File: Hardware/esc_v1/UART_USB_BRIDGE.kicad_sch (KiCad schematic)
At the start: 11 parts, among them U5 CP2102N-Axx-xQFN24

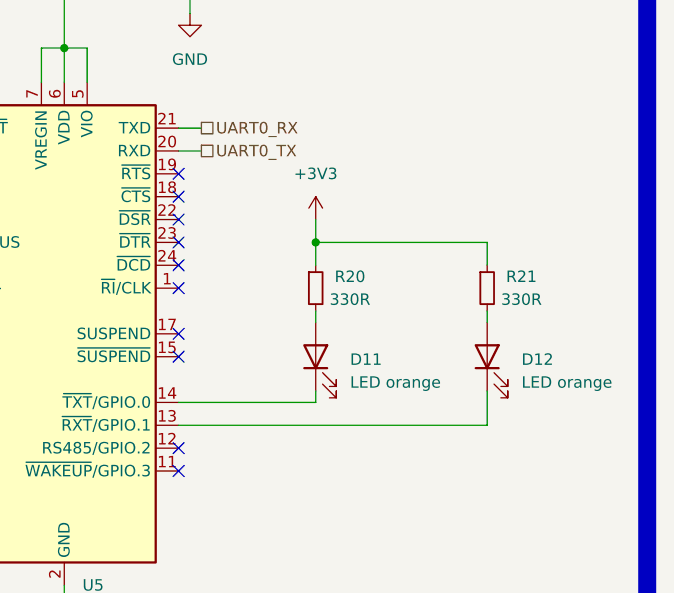
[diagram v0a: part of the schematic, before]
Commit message: changed gate driver, removed 10V buck and 5V LDO, added 5V buck. Started on Layout
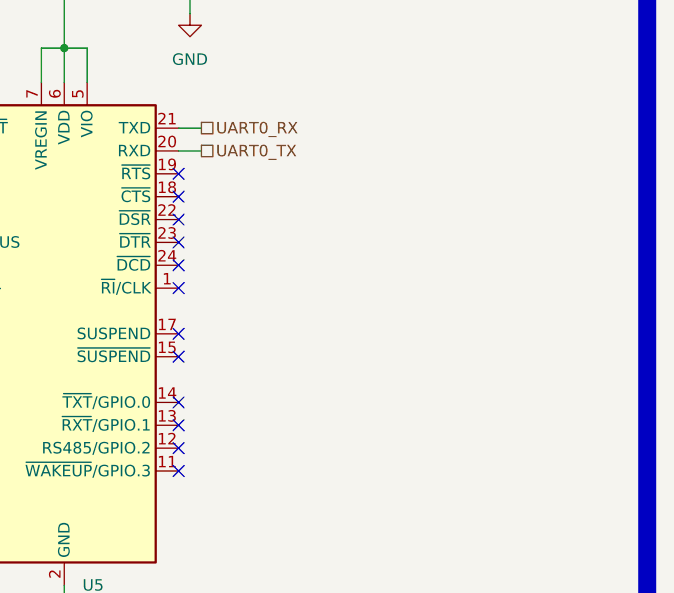
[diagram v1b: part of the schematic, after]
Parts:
- removed D11, D12: LED orange, LED_SMD:LED_0603_1608Metric, symbol Device:LED
- removed R20, R21: 330R, Resistor_SMD:R_0603_1608Metric, symbol Device:R_Small
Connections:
- no-connect marks 10 -> 12
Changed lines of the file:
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@@
   (title_block
     (title "UART to USB bridge")
-    (date "2022-07-21")
+    (date "2022-08-13")
     (rev "1")
-  )
-  (junction (at 179.07 95.25) (diameter 0) (color 0 0 0 0)
   )
   (junction (at 151.13 73.66) (diameter 0) (color 0 0 0 0)
@@
   (no_connect (at 163.83 120.65))
   (no_connect (at 163.83 118.11))
+  (no_connect (at 163.83 115.57))
+  (no_connect (at 163.83 113.03))
   (no_connect (at 163.83 107.95))
   (no_connect (at 163.83 92.71))
@@
   (no_connect (at 163.83 105.41))
   (no_connect (at 163.83 100.33))
-  (wire (pts (xy 198.12 115.57) (xy 198.12 111.76))
-    (stroke (width 0) (type default) (color 0 0 0 0))
-  )
   (wire (pts (xy 158.75 54.61) (xy 171.45 54.61))
     (stroke (width 0) (type default) (color 0 0 0 0))
@@
     (stroke (width 0) (type default) (color 0 0 0 0))
   )
-  (wire (pts (xy 163.83 115.57) (xy 198.12 115.57))
-    (stroke (width 0) (type default) (color 0 0 0 0))
-  )
   (polyline (pts (xy 38.1 38.1) (xy 38.1 73.66))
     (stroke (width 2) (type solid) (color 0 0 0 0))
   )
-  (wire (pts (xy 179.07 111.76) (xy 179.07 113.03))
-    (stroke (width 0) (type default) (color 0 0 0 0))
-  )
-  (wire (pts (xy 198.12 95.25) (xy 198.12 97.79))
-    (stroke (width 0) (type default) (color 0 0 0 0))
-  )
   (wire (pts (xy 113.03 85.09) (xy 118.11 85.09))
     (stroke (width 0) (type default) (color 0 0 0 0))
@@
     (stroke (width 2) (type solid) (color 0 0 0 0))
   )
-  (wire (pts (xy 179.07 113.03) (xy 163.83 113.03))
-    (stroke (width 0) (type default) (color 0 0 0 0))
-  )
   (wire (pts (xy 55.88 54.61) (xy 55.88 52.07))
     (stroke (width 0) (type default) (color 0 0 0 0))
   )
-  (wire (pts (xy 179.07 95.25) (xy 198.12 95.25))
-    (stroke (width 0) (type default) (color 0 0 0 0))
-  )
   (polyline (pts (xy 215.9 152.4) (xy 215.9 38.1))
     (stroke (width 2) (type solid) (color 0 0 0 0))
   )
-  (wire (pts (xy 198.12 102.87) (xy 198.12 104.14))
-    (stroke (width 0) (type default) (color 0 0 0 0))
-  )
   (wire (pts (xy 135.89 62.23) (xy 135.89 82.55))
     (stroke (width 0) (type default) (color 0 0 0 0))
@@
     (stroke (width 0) (type default) (color 0 0 0 0))
   )
-  (wire (pts (xy 179.07 95.25) (xy 179.07 97.79))
-    (stroke (width 0) (type default) (color 0 0 0 0))
-  )
   (wire (pts (xy 163.83 82.55) (xy 166.37 82.55))
     (stroke (width 0) (type default) (color 0 0 0 0))
@@
     (stroke (width 0) (type default) (color 0 0 0 0))
   )
-  (wire (pts (xy 179.07 102.87) (xy 179.07 104.14))
-    (stroke (width 0) (type default) (color 0 0 0 0))
-  )
   (wire (pts (xy 135.89 97.79) (xy 138.43 97.79))
     (stroke (width 0) (type default) (color 0 0 0 0))
   )
   (wire (pts (xy 135.89 100.33) (xy 138.43 100.33))
-    (stroke (width 0) (type default) (color 0 0 0 0))
-  )
-  (wire (pts (xy 179.07 92.71) (xy 179.07 95.25))
     (stroke (width 0) (type default) (color 0 0 0 0))
   )
@@
     )
     (property "Datasheet" "~" (id 3) (at 118.11 88.9 0)
-      (effects (font (size 1.27 1.27)) hide)
-    )
-    (pin "1")
-    (pin "2")
-  )
-  (symbol (lib_id "Device:LED") (at 179.07 107.95 90) (unit 1)
-    (in_bom yes) (on_board yes) (fields_autoplaced)
-    (property "Reference" "D11" (id 0) (at 182.88 108.2674 90)
-      (effects (font (size 1.27 1.27)) (justify right))
-    )
-    (property "Value" "LED orange" (id 1) (at 182.88 110.8074 90)
-      (effects (font (size 1.27 1.27)) (justify right))
-    )
-    (property "Footprint" "LED_SMD:LED_0603_1608Metric" (id 2) (at 179.07 107.95 0)
-      (effects (font (size 1.27 1.27)) hide)
-    )
-    (property "Datasheet" "~" (id 3) (at 179.07 107.95 0)
-      (effects (font (size 1.27 1.27)) hide)
-    )
-    (pin "1")
-    (pin "2")
-  )
-  (symbol (lib_id "Device:LED") (at 198.12 107.95 90) (unit 1)
-    (in_bom yes) (on_board yes) (fields_autoplaced)
-    (property "Reference" "D12" (id 0) (at 201.93 108.2674 90)
-      (effects (font (size 1.27 1.27)) (justify right))
-    )
-    (property "Value" "LED orange" (id 1) (at 201.93 110.8074 90)
-      (effects (font (size 1.27 1.27)) (justify right))
-    )
-    (property "Footprint" "LED_SMD:LED_0603_1608Metric" (id 2) (at 198.12 107.95 0)
-      (effects (font (size 1.27 1.27)) hide)
-    )
-    (property "Datasheet" "~" (id 3) (at 198.12 107.95 0)
       (effects (font (size 1.27 1.27)) hide)
     )
@@
     (pin "1")
   )
-  (symbol (lib_id "power:+3V3") (at 179.07 92.71 0) (unit 1)
-    (in_bom yes) (on_board yes) (fields_autoplaced)
-    (property "Reference" "#PWR077" (id 0) (at 179.07 96.52 0)
-      (effects (font (size 1.27 1.27)) hide)
-    )
-    (property "Value" "+3V3" (id 1) (at 179.07 87.63 0))
-    (property "Footprint" "" (id 2) (at 179.07 92.71 0)
-      (effects (font (size 1.27 1.27)) hide)
-    )
-    (property "Datasheet" "" (id 3) (at 179.07 92.71 0)
-      (effects (font (size 1.27 1.27)) hide)
-    )
-    (pin "1")
-  )
-  (symbol (lib_id "Device:R_Small") (at 198.12 100.33 0) (unit 1)
-    (in_bom yes) (on_board yes)
-    (property "Reference" "R21" (id 0) (at 201.93 99.06 0))
-    (property "Value" "330R" (id 1) (at 201.93 101.6 0))
-    (property "Footprint" "Resistor_SMD:R_0603_1608Metric" (id 2) (at 198.12 100.33 0)
-      (effects (font (size 1.27 1.27)) hide)
-    )
-    (property "Datasheet" "~" (id 3) (at 198.12 100.33 0)
-      (effects (font (size 1.27 1.27)) hide)
-    )
-    (pin "1")
-    (pin "2")
-  )
   (symbol (lib_id "Device:C_Small") (at 158.75 59.69 0) (unit 1)
     (in_bom yes) (on_board yes)
@@
       (effects (font (size 1.27 1.27)) hide)
     )
-    (pin "1")
-    (pin "2")
-  )
-  (symbol (lib_id "Device:R_Small") (at 179.07 100.33 0) (unit 1)
-    (in_bom yes) (on_board yes)
-    (property "Reference" "R20" (id 0) (at 182.88 99.06 0))
-    (property "Value" "330R" (id 1) (at 182.88 101.6 0))
-    (property "Footprint" "Resistor_SMD:R_0603_1608Metric" (id 2) (at 179.07 100.33 0)
-      (effects (font (size 1.27 1.27)) hide)
-    )
-    (property "Datasheet" "~" (id 3) (at 179.07 100.33 0)
-      (effects (font (size 1.27 1.27)) hide)
-    )

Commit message: Removed USB to serial chip and added serial connector. Finished layout, made production files and sent to production
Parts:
- U5: Part no (none) -> CP2102N
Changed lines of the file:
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@@
+      (effects (font (size 1.27 1.27)) hide)
+    )
+    (property "Part no" "CP2102N" (id 4) (at 151.13 105.41 0)
       (effects (font (size 1.27 1.27)) hide)
     )
